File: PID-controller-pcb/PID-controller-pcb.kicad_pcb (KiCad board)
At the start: 2 copper layers, 10 parts

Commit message: touched up pcb, added a comment in code.py
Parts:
- moved ADS 37.0 mm to (207.0, 118.1)
- moved DAC 37.0 mm to (156.2, 118.1)
- moved ETH1 37.0 mm to (135.9, 50.8)
- moved Pico2 37.0 mm to (199.4, 49.5)
- moved QWIIK LCD 37.0 mm to (234.7, 102.9)
- moved CurrInBNC 37.0 mm to (240.0, 59.7)
- moved CurrOutBNC 37.0 mm to (219.7, 59.7)
- moved Pico1 37.0 mm to (181.6, 49.5)
- moved ETH2 37.0 mm to (156.2, 50.8)
- moved ThermInBNC 37.0 mm to (260.4, 59.7)
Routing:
- net (no net): track 1328.9 -> 1379.9 mm
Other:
- board outline added: 147 x 86 mm

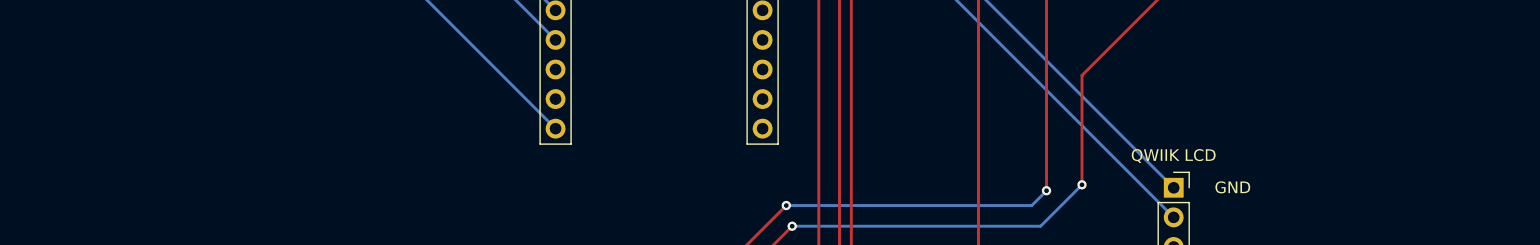
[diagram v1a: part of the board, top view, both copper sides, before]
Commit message: added screw holes on PCB
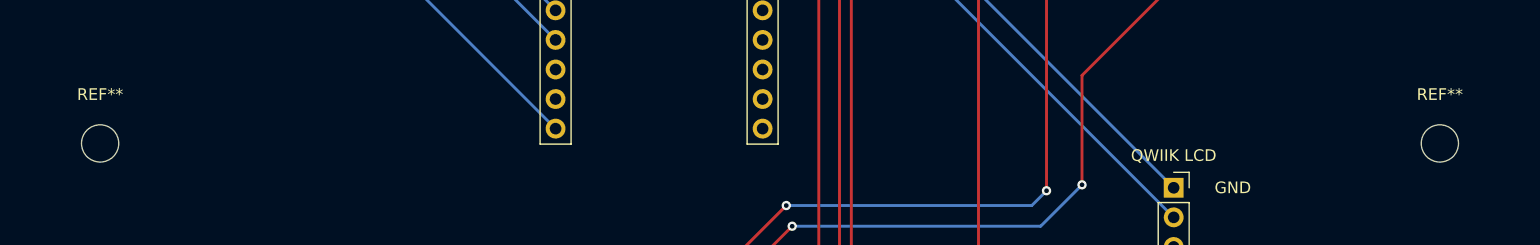
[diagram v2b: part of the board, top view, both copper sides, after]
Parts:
- added REF**: MountingHole_3.2mm_M3, MountingHole:MountingHole_3.2mm_M3, F.Cu at (142.5, 99.1)
- added REF**: MountingHole_3.2mm_M3, MountingHole:MountingHole_3.2mm_M3, F.Cu at (257.6, 99.1)

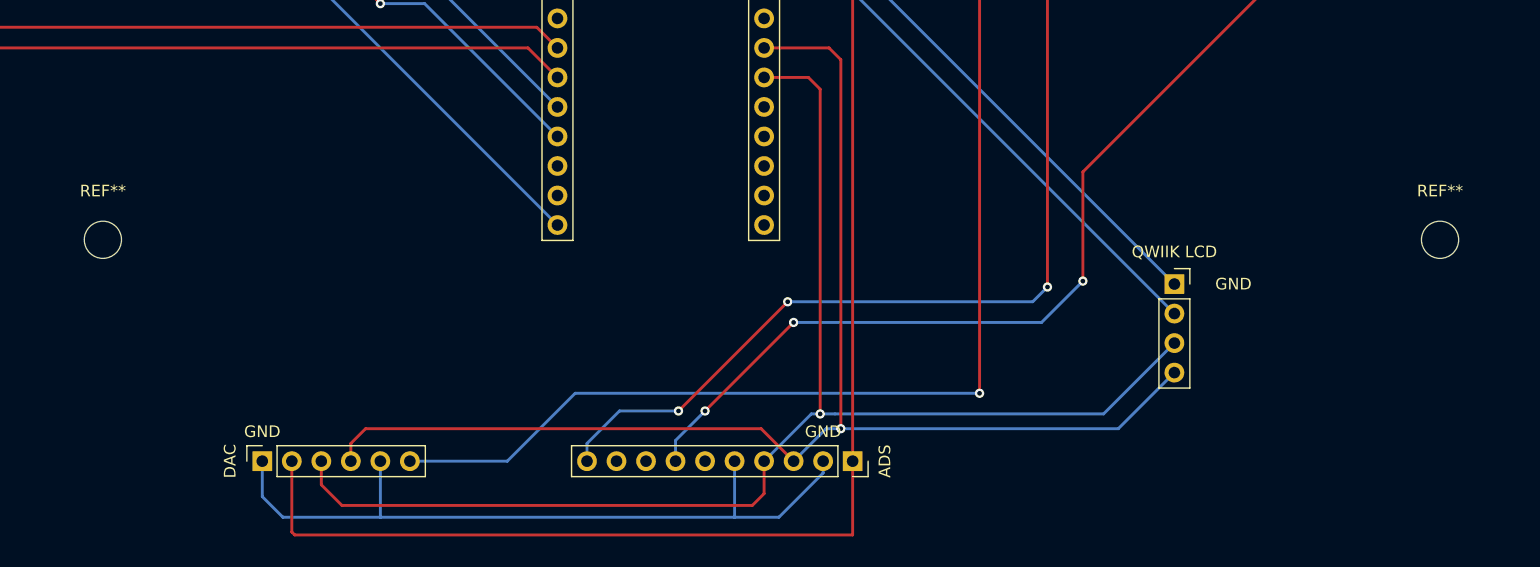
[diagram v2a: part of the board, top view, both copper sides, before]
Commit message: added more screw holes on PCB
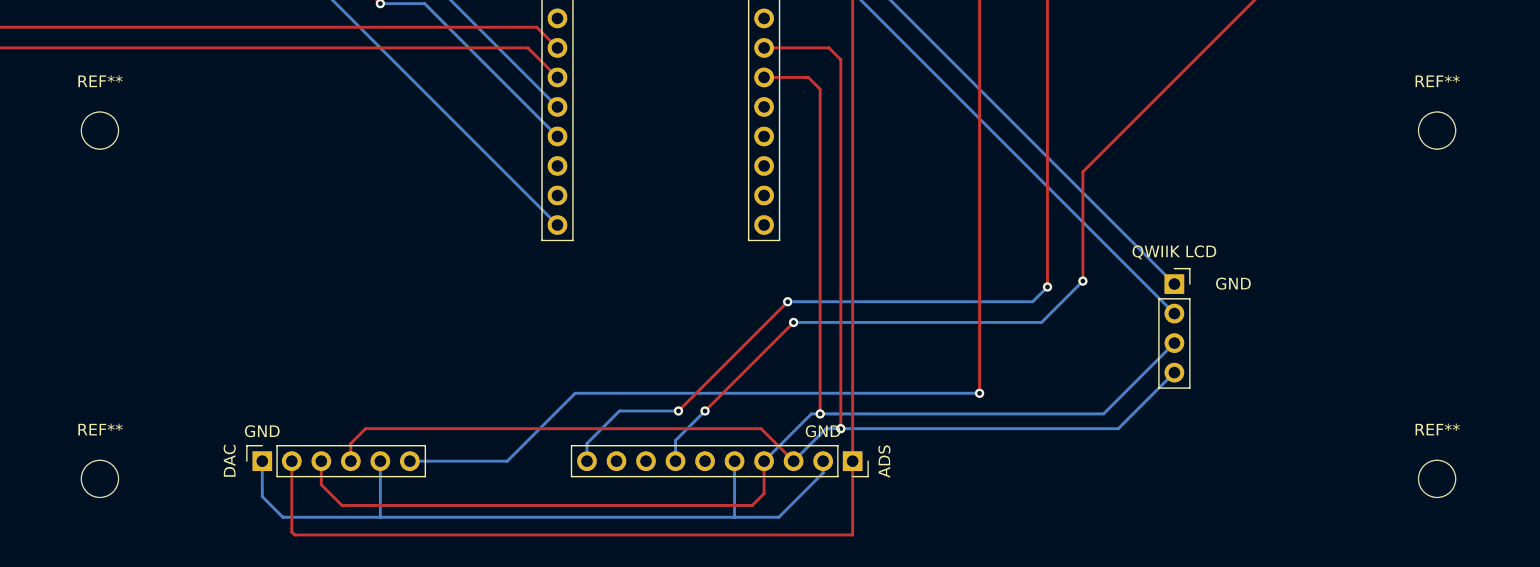
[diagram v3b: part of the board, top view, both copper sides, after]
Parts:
- added REF**: MountingHole_3.2mm_M3, MountingHole:MountingHole_3.2mm_M3, F.Cu at (142.2, 119.6)
- added REF**: MountingHole_3.2mm_M3, MountingHole:MountingHole_3.2mm_M3, F.Cu at (257.3, 119.6)
- moved REF** 9.40 mm to (142.2, 89.7)
- moved REF** 9.40 mm to (257.3, 89.7)
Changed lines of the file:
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@@
     (tracks 134)
     (zones 0)
-    (modules 12)
+    (modules 14)
     (nets 1)
   )
@@
   )
   (module MountingHole:MountingHole_3.2mm_M3 (layer F.Cu)
-    (at 142.494 99.06)
+    (at 142.24 119.634)
+    (descr "Mounting Hole 3.2mm, no annular, M3")
+    (tags "mounting hole 3.2mm no annular m3")
+    (attr virtual)
+    (fp_text reference REF** (at 0 -4.2) (layer F.SilkS)
+      (effects (font (size 1 1) (thickness 0.15)))
+    )
+    (fp_text value MountingHole_3.2mm_M3 (at 0 4.2) (layer F.Fab)
+      (effects (font (size 1 1) (thickness 0.15)))
+    )
+    (fp_circle (center 0 0) (end 3.2 0) (layer Cmts.User) (width 0.15))
+    (fp_circle (center 0 0) (end 3.45 0) (layer F.CrtYd) (width 0.05))
+    (fp_text user %R (at 0.3 0) (layer F.Fab)
+      (effects (font (size 1 1) (thickness 0.15)))
+    )
+    (pad 1 np_thru_hole circle (at 0 0) (size 3.2 3.2) (drill 3.2) (layers *.Cu *.Mask))
+  )
+  (module MountingHole:MountingHole_3.2mm_M3 (layer F.Cu)
+    (at 257.302 119.634)
+    (descr "Mounting Hole 3.2mm, no annular, M3")
+    (tags "mounting hole 3.2mm no annular m3")
+    (attr virtual)
+    (fp_text reference REF** (at 0 -4.2) (layer F.SilkS)
+      (effects (font (size 1 1) (thickness 0.15)))
+    )
+    (fp_text value MountingHole_3.2mm_M3 (at 0 4.2) (layer F.Fab)
+      (effects (font (size 1 1) (thickness 0.15)))
+    )
+    (fp_circle (center 0 0) (end 3.2 0) (layer Cmts.User) (width 0.15))
+    (fp_circle (center 0 0) (end 3.45 0) (layer F.CrtYd) (width 0.05))
+    (fp_text user %R (at 0.3 0) (layer F.Fab)
+      (effects (font (size 1 1) (thickness 0.15)))
+    )
+    (pad 1 np_thru_hole circle (at 0 0) (size 3.2 3.2) (drill 3.2) (layers *.Cu *.Mask))
+  )
+  (module MountingHole:MountingHole_3.2mm_M3 (layer F.Cu)
+    (at 142.24 89.662)
     (descr "Mounting Hole 3.2mm, no annular, M3")
     (tags "mounting hole 3.2mm no annular m3")
@@
   )
   (module MountingHole:MountingHole_3.2mm_M3 (layer F.Cu)
-    (at 257.556 99.06)
+    (at 257.302 89.662)
     (descr "Mounting Hole 3.2mm, no annular, M3")
     (tags "mounting hole 3.2mm no annular m3")

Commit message: added switch to pcb layout
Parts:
- added SW1: PinHeader_1x03_P2.54mm_Vertical, Connector_PinHeader_2.54mm:PinHeader_1x03_P2.54mm_Vertical, F.Cu at (162.1, 98.6)
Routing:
- net (no net): track 1379.9 -> 1560.6 mm
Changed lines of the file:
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@@
   (general
     (thickness 1.6)
-    (drawings 9)
-    (tracks 134)
+    (drawings 10)
+    (tracks 147)
     (zones 0)
-    (modules 14)
+    (modules 15)
     (nets 1)
   )
@@
     (uvia_drill 0.1)
   )
+  (module Connector_PinHeader_2.54mm:PinHeader_1x03_P2.54mm_Vertical (layer F.Cu)
+    (at 162.052 98.552)
+    (descr "Through hole straight pin header, 1x03, 2.54mm pitch, single row")
+    (tags "Through hole pin header THT 1x03 2.54mm single row")
+    (fp_text reference SW1 (at 0 -2.33) (layer F.SilkS)
+      (effects (font (size 1 1) (thickness 0.15)))
+    )
+    (fp_text value PinHeader_1x03_P2.54mm_Vertical (at 0 7.41) (layer F.Fab)
+      (effects (font (size 1 1) (thickness 0.15)))
+    )
+    (fp_text user %R (at 0 2.54 90) (layer F.Fab)
+      (effects (font (size 1 1) (thickness 0.15)))
+    )
+    (fp_line (start -0.635 -1.27) (end 1.27 -1.27) (layer F.Fab) (width 0.1))
+    (fp_line (start 1.27 -1.27) (end 1.27 6.35) (layer F.Fab) (width 0.1))
+    (fp_line (start 1.27 6.35) (end -1.27 6.35) (layer F.Fab) (width 0.1))
+    (fp_line (start -1.27 6.35) (end -1.27 -0.635) (layer F.Fab) (width 0.1))
+    (fp_line (start -1.27 -0.635) (end -0.635 -1.27) (layer F.Fab) (width 0.1))
+    (fp_line (start -1.33 6.41) (end 1.33 6.41) (layer F.SilkS) (width 0.12))
+    (fp_line (start -1.33 1.27) (end -1.33 6.41) (layer F.SilkS) (width 0.12))
+    (fp_line (start 1.33 1.27) (end 1.33 6.41) (layer F.SilkS) (width 0.12))
+    (fp_line (start -1.33 1.27) (end 1.33 1.27) (layer F.SilkS) (width 0.12))
+    (fp_line (start -1.33 0) (end -1.33 -1.33) (layer F.SilkS) (width 0.12))
+    (fp_line (start -1.33 -1.33) (end 0 -1.33) (layer F.SilkS) (width 0.12))
+    (fp_line (start -1.8 -1.8) (end -1.8 6.85) (layer F.CrtYd) (width 0.05))
+    (fp_line (start -1.8 6.85) (end 1.8 6.85) (layer F.CrtYd) (width 0.05))
+    (fp_line (start 1.8 6.85) (end 1.8 -1.8) (layer F.CrtYd) (width 0.05))
+    (fp_line (start 1.8 -1.8) (end -1.8 -1.8) (layer F.CrtYd) (width 0.05))
+    (pad 3 thru_hole oval (at 0 5.08) (size 1.7 1.7) (drill 1) (layers *.Cu *.Mask))
+    (pad 2 thru_hole oval (at 0 2.54) (size 1.7 1.7) (drill 1) (layers *.Cu *.Mask))
+    (pad 1 thru_hole rect (at 0 0) (size 1.7 1.7) (drill 1) (layers *.Cu *.Mask))
+    (model ${KISYS3DMOD}/Connector_PinHeader_2.54mm.3dshapes/PinHeader_1x03_P2.54mm_Vertical.wrl
+      (at (xyz 0 0 0))
+      (scale (xyz 1 1 1))
+      (rotate (xyz 0 0 0))
+    )
+  )
   (module MountingHole:MountingHole_3.2mm_M3 (layer F.Cu)
     (at 142.24 119.634)
@@
       (rotate (xyz 0 0 0))
     )
+  )
+  (gr_text GND (at 165.354 98.552) (layer F.SilkS)
+    (effects (font (size 1 1) (thickness 0.15)))
   )
   (gr_line (start 273 45) (end 273 131) (layer Edge.Cuts) (width 0.05))
@@
   (segment (start 163.322 53.34) (end 156.21 53.34) (width 0.25) (layer B.Cu) (net 0))
   (segment (start 169.672 46.99) (end 163.322 53.34) (width 0.25) (layer B.Cu) (net 0))
+  (segment (start 191.008 53.34) (end 191.008 98.298) (width 0.25) (layer B.Cu) (net 0))
+  (segment (start 191.008 98.298) (end 185.674 103.632) (width 0.25) (layer B.Cu) (net 0))
+  (segment (start 185.674 103.632) (end 164.084 103.632) (width 0.25) (layer B.Cu) (net 0))
+  (segment (start 156.21 118.11) (end 156.21 99.568) (width 0.25) (layer F.Cu) (net 0))
+  (segment (start 156.21 99.568) (end 157.226 98.552) (width 0.25) (layer F.Cu) (net 0))
+  (segment (start 157.226 98.552) (end 162.052 98.552) (width 0.25) (layer F.Cu) (net 0))
+  (segment (start 162.306 101.346) (end 162.052 101.092) (width 0.25) (layer F.Cu) (net 0))
+  (segment (start 184.658 101.346) (end 162.306 101.346) (width 0.25) (layer F.Cu) (net 0))
+  (segment (start 187.96 98.044) (end 184.658 101.346) (width 0.25) (layer F.Cu) (net 0))
+  (segment (start 187.96 53.848) (end 187.96 98.044) (width 0.25) (layer F.Cu) (net 0))
+  (segment (start 183.642 49.53) (end 187.96 53.848) (width 0.25) (layer F.Cu) (net 0))
+  (segment (start 181.61 49.53) (end 183.642 49.53) (width 0.25) (layer F.Cu) (net 0))
+  (segment (start 164.084 103.632) (end 162.052 103.632) (width 0.25) (layer B.Cu) (net 0))
 )

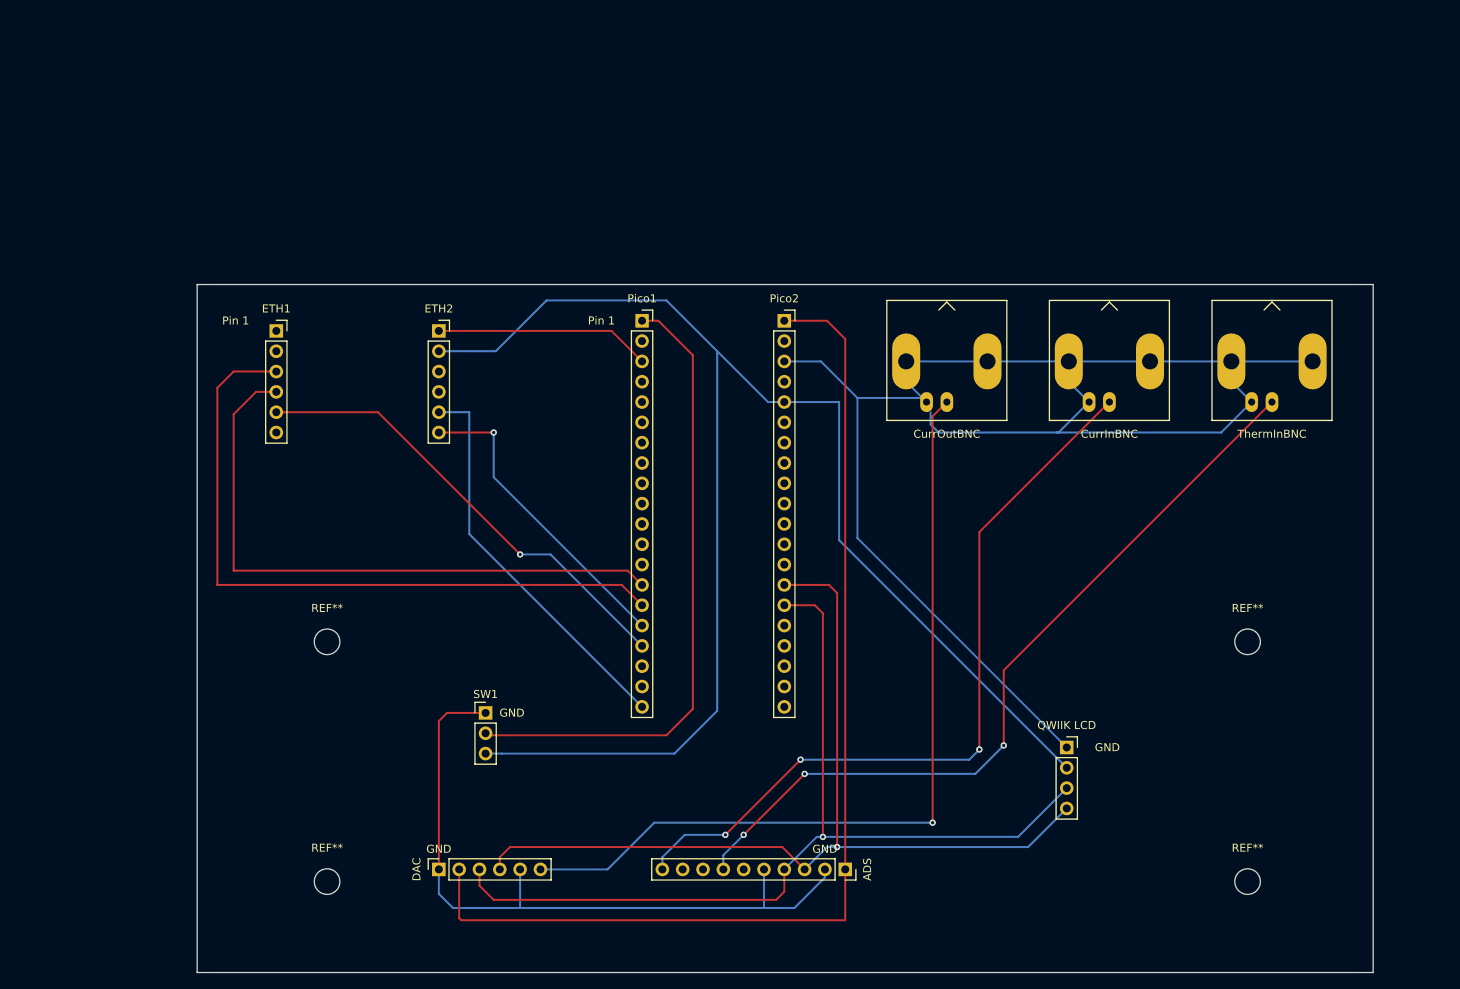
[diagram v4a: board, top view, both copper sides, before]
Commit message: seperated grounds, slightly reworked design
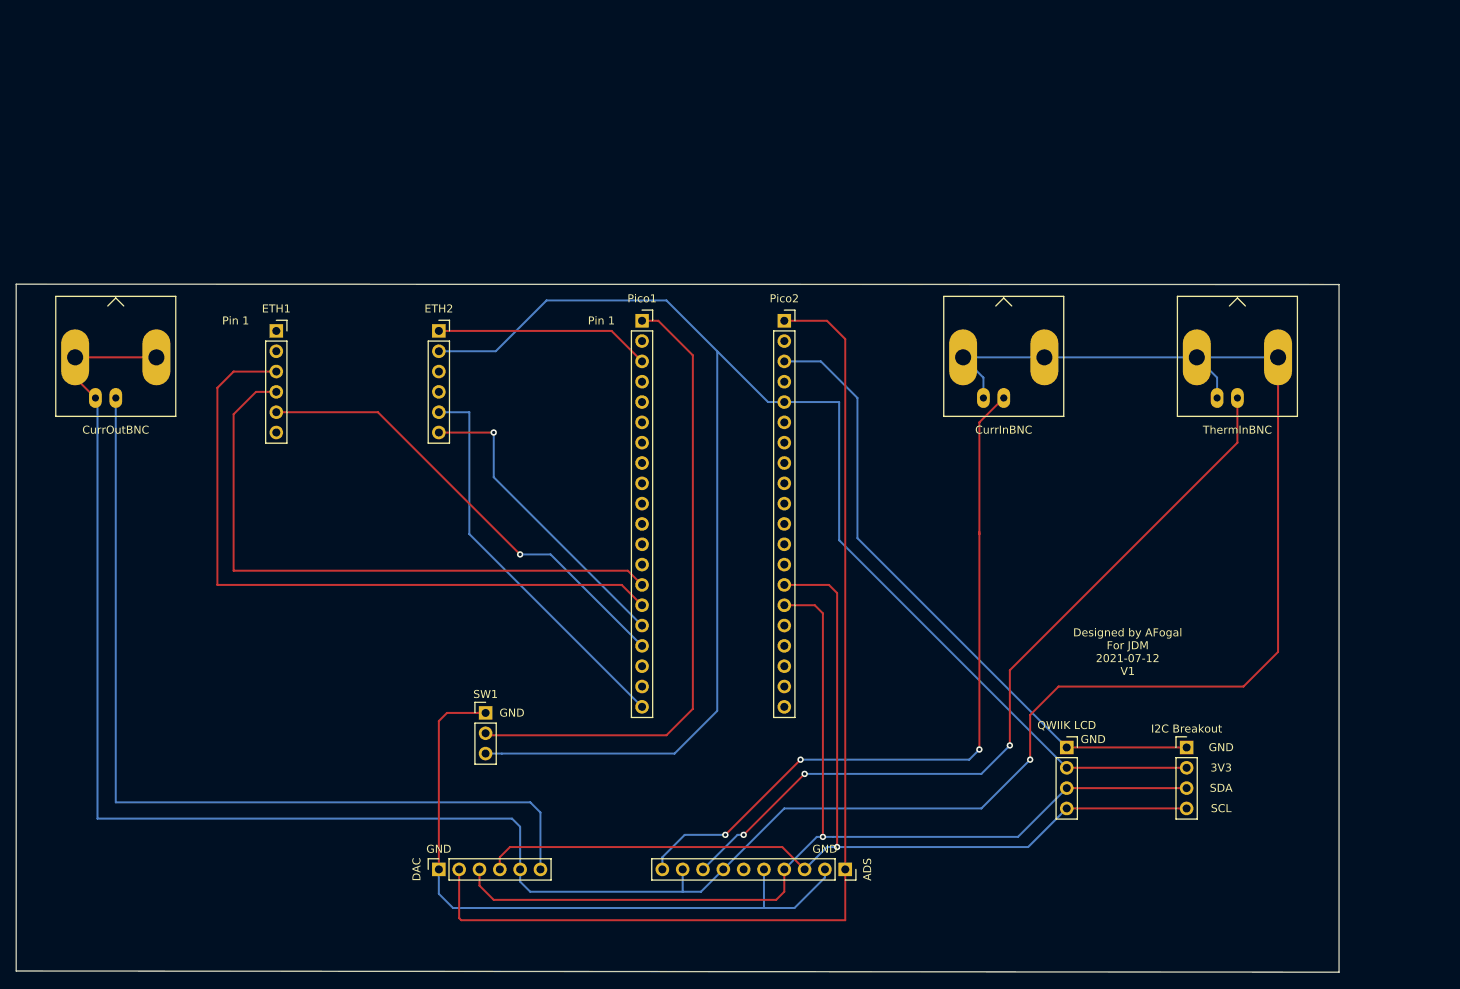
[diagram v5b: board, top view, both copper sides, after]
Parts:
- removed REF** (x4): MountingHole_3.2mm_M3, MountingHole:MountingHole_3.2mm_M3
- added I2C Breakout: PinHeader_1x04_P2.54mm_Vertical, Connector_PinHeader_2.54mm:PinHeader_1x04_P2.54mm_Vertical, F.Cu at (249.7, 102.9)
- moved CurrOutBNC 103.9 mm to (115.8, 59.2)
- moved CurrInBNC 13.2 mm to (226.8, 59.2)
- moved ThermInBNC 4.35 mm to (256.0, 59.2)
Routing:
- net (no net): track 1560.6 -> 1822.1 mm
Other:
- board size 147 x 86 mm -> 165.4 x 86 mm
- board text added: "3V3"
- board text added: "Designed by AFogal For JDM 2021-07-12 V1"
- board text added: "SCL"
- board text added: "SDA"
